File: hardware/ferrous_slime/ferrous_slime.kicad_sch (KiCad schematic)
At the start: 50 parts, among them J1 IMU_Connector, J2 Battery_Connector, J3 USB_C_Receptacle_USB2.0, Q1 DMG3415U, SW1 SW_PWR, U1 BNO/MPU/ICM_Break, U2 ESP32-C3-MINI-1, U3 TP4056, U4 M3406, Y1 32.768Hz

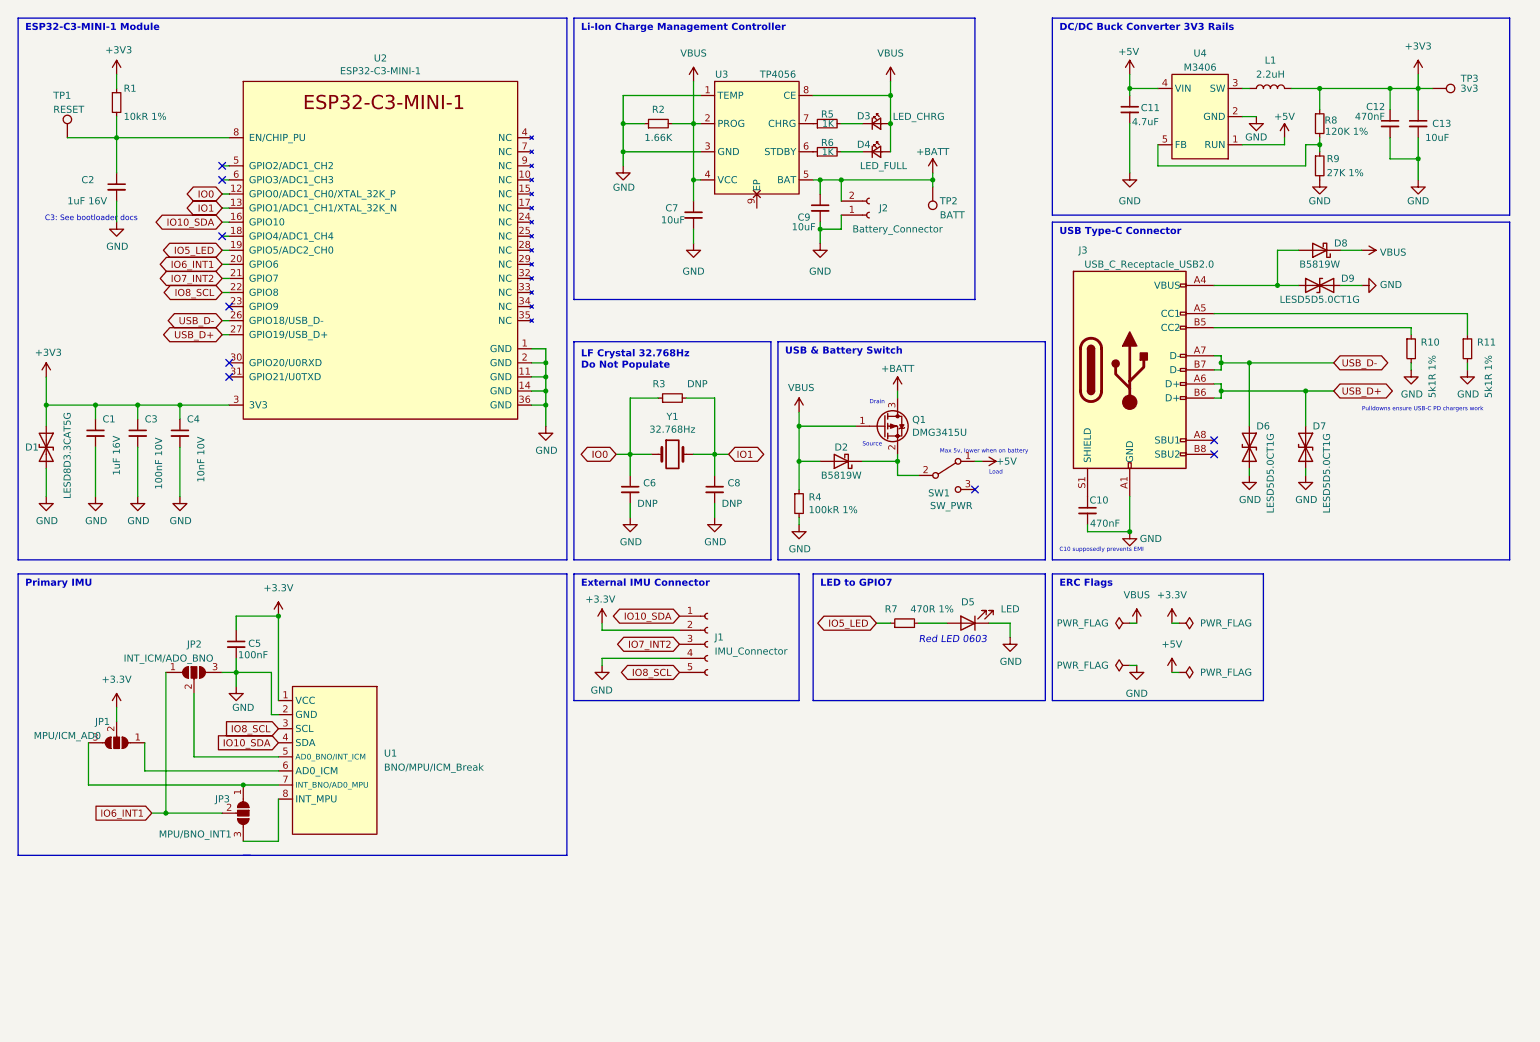
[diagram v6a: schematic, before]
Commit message: Added battery sense to ferrous_slime
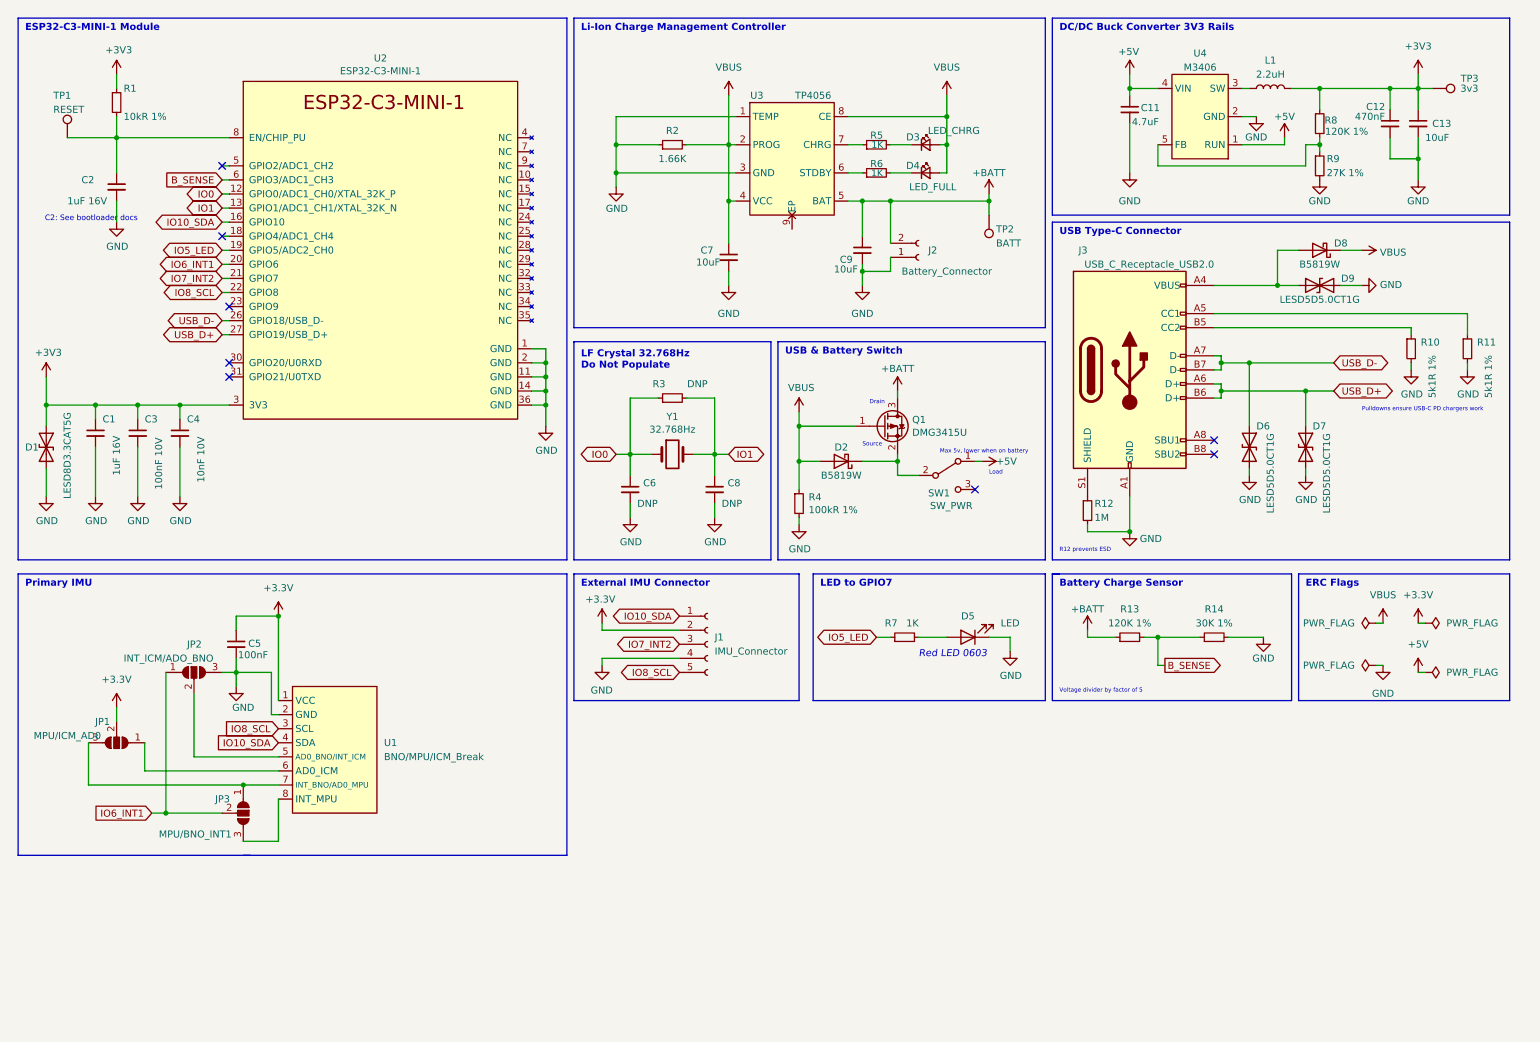
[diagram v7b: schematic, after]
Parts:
- removed C10: 470nF, Capacitor_SMD:C_0603_1608Metric, symbol Device:C_Small
- added R12: 1M, Resistor_SMD:R_0603_1608Metric, symbol Device:R_Small
- added R13: 120K 1%, Resistor_SMD:R_0603_1608Metric, symbol Device:R_Small
- added R14: 30K 1%, Resistor_SMD:R_0603_1608Metric, symbol Device:R_Small
- R7: value 470R 1% -> 1K
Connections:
- net +BATT: now also R13.1
- net GND: now also R12.2, R14.2
- net at J3.S1 (SHIELD): now also R12.1
- net B_SENSE: now reaches U2.6 (GPIO3/ADC1_CH3)
- net B_SENSE: now also R13.2, R14.1
- no-connect marks 9 -> 8
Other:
- note added: "Battery Charge Sensor"
- note added: "C2: See bootloader docs"
- note added: "R12 prevents ESD"
- note added: "Voltage divider by factor of 5"
- note removed: "C10 supposedly prevents EMI"
- note removed: "C3: See bootloader docs"
- moved on the sheet: C7, C9, D3, D4, D5, J2, R2, R5, R6, R7, TP2, U1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

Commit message: Added breakouts for remaining unused IO
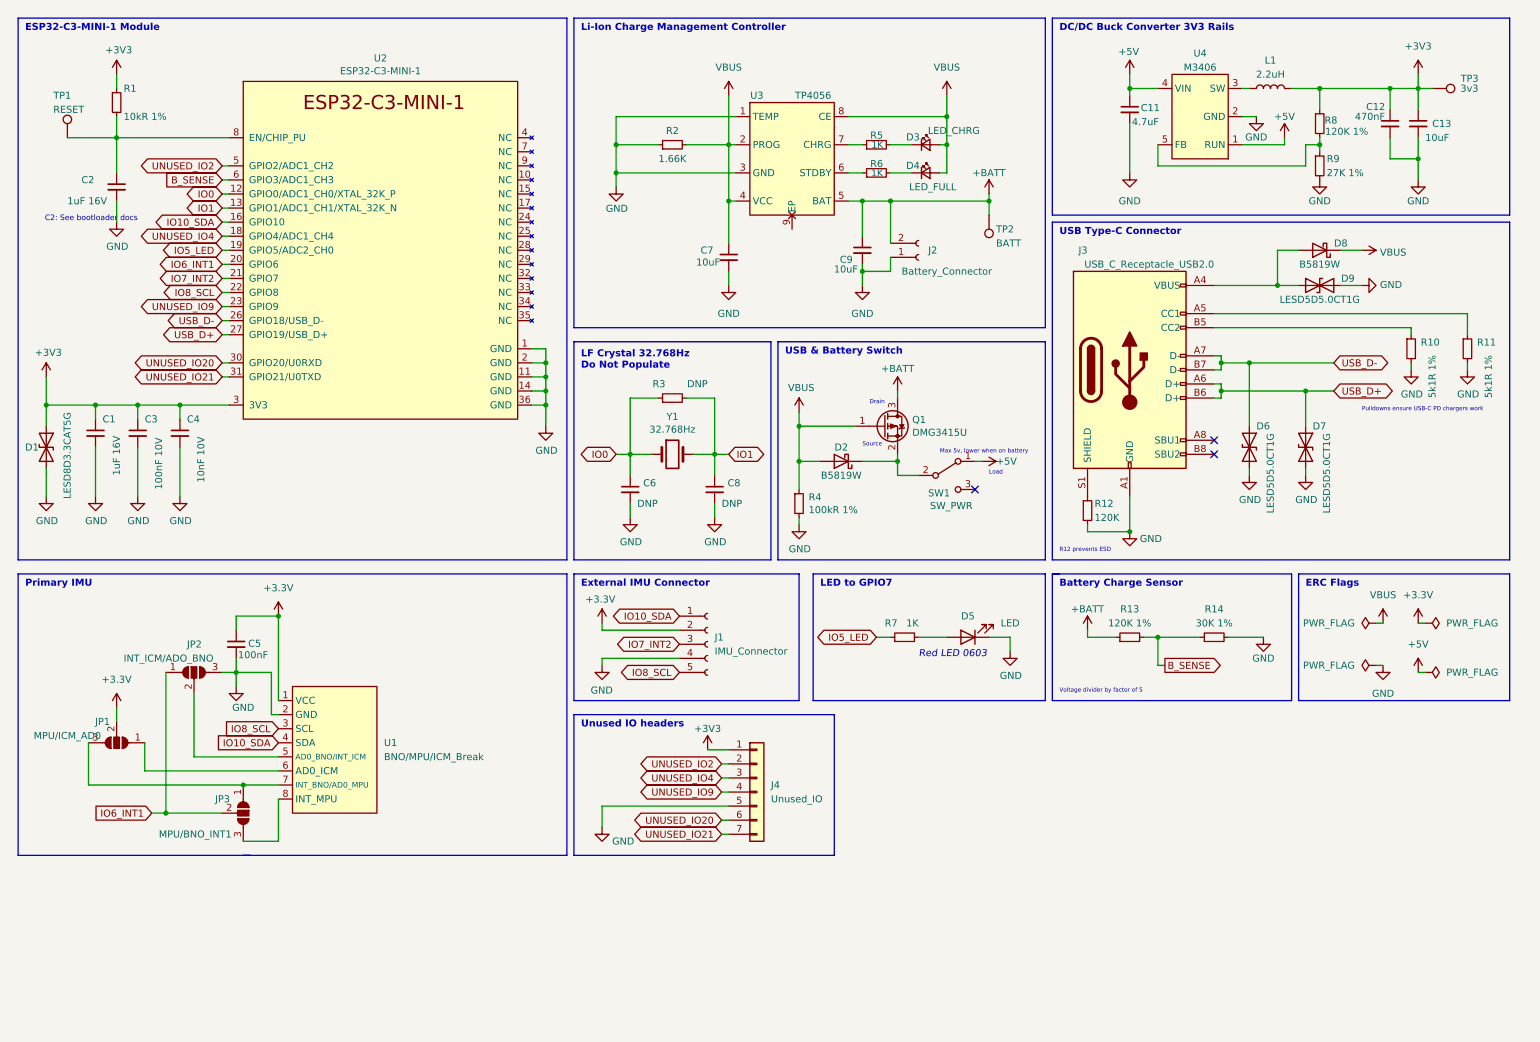
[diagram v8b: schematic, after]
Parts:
- added J4: Unused_IO, Connector_PinHeader_2.54mm:PinHeader_1x07_P2.54mm_Vertical, symbol Connector_Generic:Conn_01x07
- R12: value 1M -> 120K
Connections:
- net +3V3: now also J4.1 (Pin_1)
- net GND: now also J4.5 (Pin_5)
- net UNUSED_IO4: now reaches U2.18 (GPIO4/ADC1_CH4)
- net UNUSED_IO4: now also J4.3 (Pin_3)
- net UNUSED_IO9: now reaches U2.23 (GPIO9)
- net UNUSED_IO9: now also J4.4 (Pin_4)
- net UNUSED_IO20: now reaches U2.30 (GPIO20/U0RXD)
- net UNUSED_IO20: now also J4.6 (Pin_6)
- net UNUSED_IO21: now reaches U2.31 (GPIO21/U0TXD)
- net UNUSED_IO21: now also J4.7 (Pin_7)
- net UNUSED_IO2: now reaches U2.5 (GPIO2/ADC1_CH2)
- net UNUSED_IO2: now also J4.2 (Pin_2)
- no-connect marks 8 -> 3
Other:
- note added: "Unused IO headers"
